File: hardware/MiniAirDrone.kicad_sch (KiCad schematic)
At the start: 26 parts, among them J1 USB_C_Receptacle_USB2.0, Q1 UMH3N, U1 CH340C, U2 ESP32-WROOM-32, U3 MPU-6050, U4 MS5611-01BA, U5 VL53L1CXV0FY1, U6 TS1117BCW33_RPG

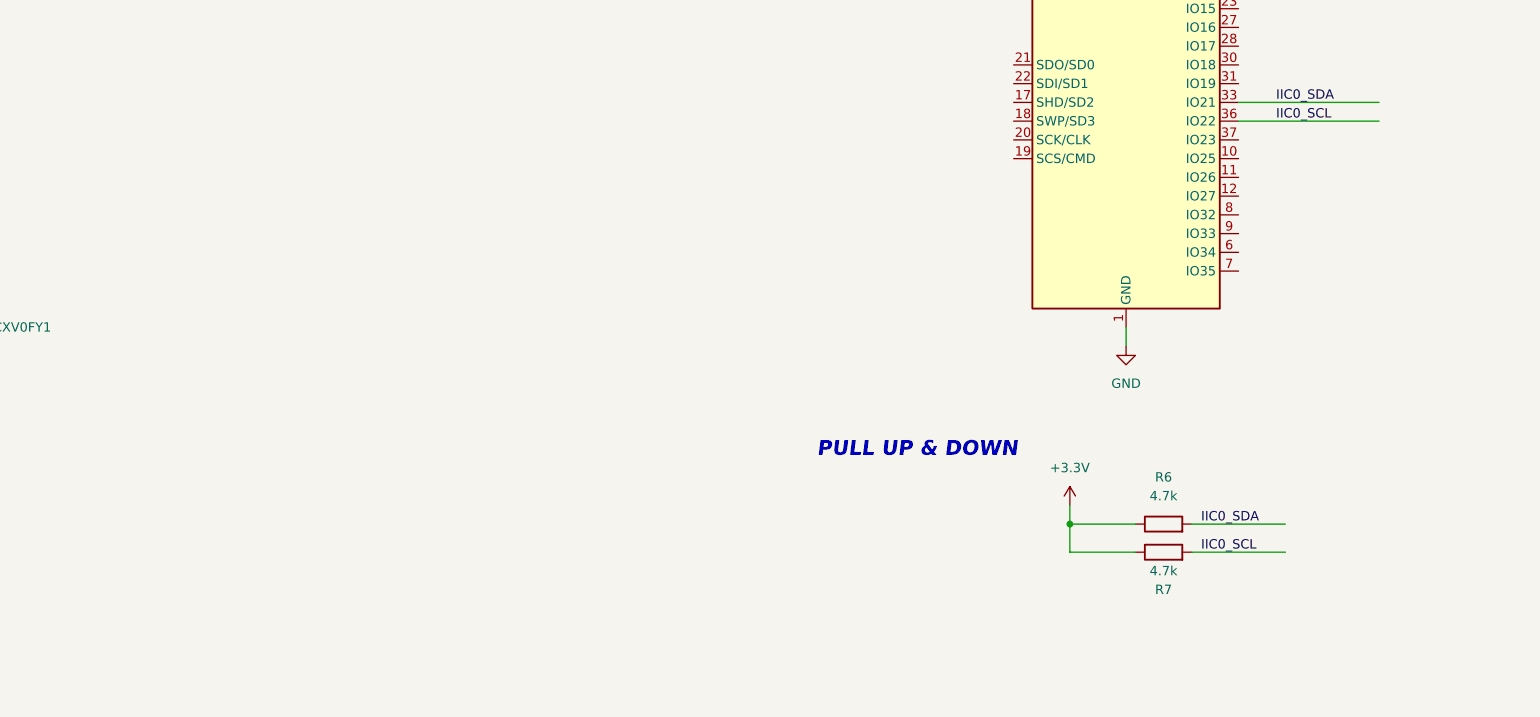
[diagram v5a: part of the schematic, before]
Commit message: new footprint and symbol
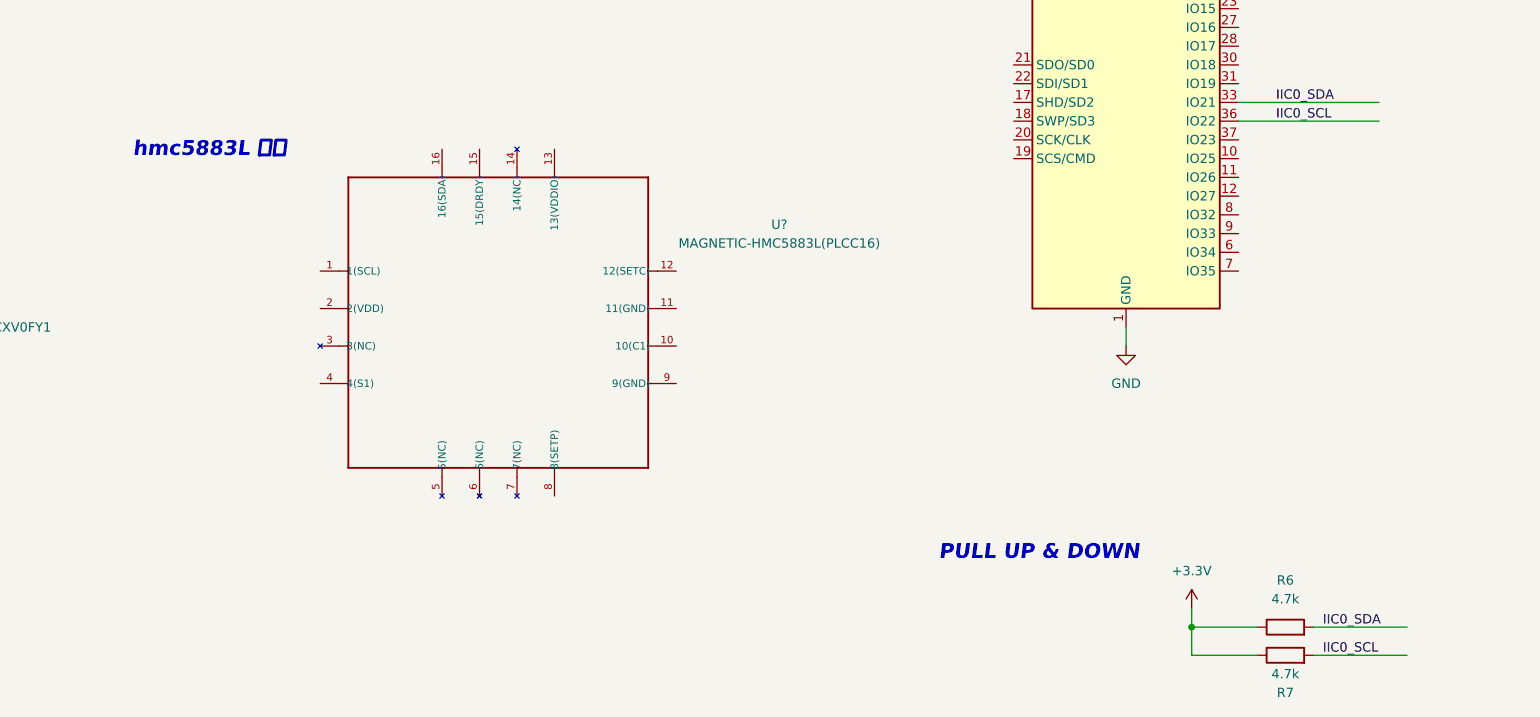
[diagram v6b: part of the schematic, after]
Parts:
- added U?: MAGNETIC-HMC5883L(PLCC16), PLCC16-0.5-3X3MM, symbol HMC5883L:MAGNETIC-HMC5883L(PLCC16)
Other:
- note added: "hmc5883L 罗盘"
- moved on the sheet: R6, R7
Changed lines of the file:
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@@
   (junction (at 49.53 41.91) (diameter 0) (color 0 0 0 0)
   )
-  (junction (at 350.52 134.62) (diameter 0) (color 0 0 0 0)
+  (junction (at 367.03 148.59) (diameter 0) (color 0 0 0 0)
   )
   (junction (at 116.84 91.44) (diameter 0) (color 0 0 0 0)
@@
     (stroke (width 0) (type default) (color 0 0 0 0))
   )
-  (wire (pts (xy 350.52 132.08) (xy 350.52 134.62))
+  (wire (pts (xy 367.03 146.05) (xy 367.03 148.59))
     (stroke (width 0) (type default) (color 0 0 0 0))
   )
@@
     (stroke (width 0) (type default) (color 0 0 0 0))
   )
-  (wire (pts (xy 367.03 134.62) (xy 379.73 134.62))
+  (wire (pts (xy 383.54 148.59) (xy 396.24 148.59))
     (stroke (width 0) (type default) (color 0 0 0 0))
   )
@@
     (stroke (width 0) (type default) (color 0 0 0 0))
   )
-  (wire (pts (xy 367.03 138.43) (xy 379.73 138.43))
+  (wire (pts (xy 383.54 152.4) (xy 396.24 152.4))
     (stroke (width 0) (type default) (color 0 0 0 0))
   )
@@
     (stroke (width 0) (type default) (color 0 0 0 0))
   )
-  (wire (pts (xy 350.52 134.62) (xy 359.41 134.62))
+  (wire (pts (xy 367.03 148.59) (xy 375.92 148.59))
     (stroke (width 0) (type default) (color 0 0 0 0))
   )
@@
     (stroke (width 0) (type default) (color 0 0 0 0))
   )
-  (wire (pts (xy 350.52 138.43) (xy 350.52 134.62))
+  (wire (pts (xy 367.03 152.4) (xy 367.03 148.59))
     (stroke (width 0) (type default) (color 0 0 0 0))
   )
@@
     (stroke (width 0) (type default) (color 0 0 0 0))
   )
-  (wire (pts (xy 359.41 138.43) (xy 350.52 138.43))
+  (wire (pts (xy 375.92 152.4) (xy 367.03 152.4))
     (stroke (width 0) (type default) (color 0 0 0 0))
   )
@@
     (effects (font (size 1.27 1.27)) (justify left bottom))
   )
+  (text "hmc5883L 罗盘" (at 223.52 85.09 0)
+    (effects (font (size 2.0066 2.0066) (thickness 0.4013) bold italic) (justify left bottom))
+  )
   (text "USB" (at 17.78 20.32 0)
     (effects (font (size 2.0066 2.0066) (thickness 0.4013) bold italic) (justify left bottom))
   )
-  (text "PULL UP & DOWN" (at 316.23 125.73 0)
+  (text "PULL UP & DOWN" (at 332.74 139.7 0)
     (effects (font (size 2.0066 2.0066) (thickness 0.4013) bold italic) (justify left bottom))
   )
@@
     (effects (font (size 1.27 1.27)) (justify left bottom))
   )
-  (label "IIC0_SDA" (at 368.3 134.62 0)
+  (label "IIC0_SDA" (at 384.81 148.59 0)
     (effects (font (size 1.27 1.27)) (justify left bottom))
   )
-  (label "IIC0_SCL" (at 368.3 138.43 0)
+  (label "IIC0_SCL" (at 384.81 152.4 0)
     (effects (font (size 1.27 1.27)) (justify left bottom))
   )
@@
     (pin "2")
   )
-  (symbol (lib_id "Device:R") (at 363.22 138.43 90) (unit 1)
-    (in_bom yes) (on_board yes)
-    (property "Reference" "R7" (id 0) (at 363.22 143.51 90))
-    (property "Value" "4.7k" (id 1) (at 363.22 140.97 90))
-    (property "Footprint" "" (id 2) (at 363.22 140.208 90)
-      (effects (font (size 1.27 1.27)) hide)
-    )
-    (property "Datasheet" "~" (id 3) (at 363.22 138.43 0)
+  (symbol (lib_id "Device:R") (at 379.73 152.4 90) (unit 1)
+    (in_bom yes) (on_board yes)
+    (property "Reference" "R7" (id 0) (at 379.73 157.48 90))
+    (property "Value" "4.7k" (id 1) (at 379.73 154.94 90))
+    (property "Footprint" "" (id 2) (at 379.73 154.178 90)
+      (effects (font (size 1.27 1.27)) hide)
+    )
+    (property "Datasheet" "~" (id 3) (at 379.73 152.4 0)
       (effects (font (size 1.27 1.27)) hide)
     )
@@
     )
     (pin "1")
+  )
+  (symbol (lib_id "HMC5883L:MAGNETIC-HMC5883L(PLCC16)") (at 273.05 107.95 0) (unit 1)
+    (in_bom yes) (on_board yes) (fields_autoplaced)
+    (property "Reference" "U?" (id 0) (at 311.15 94.0306 0))
+    (property "Value" "MAGNETIC-HMC5883L(PLCC16)" (id 1) (at 311.15 96.5706 0))
+    (property "Footprint" "PLCC16-0.5-3X3MM" (id 2) (at 273.05 107.95 0)
+      (effects (font (size 1.27 1.27)) (justify left bottom) hide)
+    )
+    (property "Datasheet" "" (id 3) (at 273.05 107.95 0)
+      (effects (font (size 1.27 1.27)) (justify left bottom) hide)
+    )
+    (property "MPN" "HMC5883L" (id 4) (at 273.05 107.95 0)
+      (effects (font (size 1.27 1.27)) (justify left bottom) hide)
+    )
+    (property "VALUE" "HMC5883L" (id 5) (at 273.05 107.95 0)
+      (effects (font (size 1.27 1.27)) (justify left bottom) hide)
+    )
+    (pin "1")
+    (pin "10")
+    (pin "11")
+    (pin "12")
+    (pin "13")
+    (pin "14")
+    (pin "15")
+    (pin "16")
+    (pin "2")
+    (pin "3")
+    (pin "4")
+    (pin "5")
+    (pin "6")
+    (pin "7")
+    (pin "8")
+    (pin "9")
   )
   (symbol (lib_id "Device:C_Small") (at 339.09 27.94 0) (unit 1)
@@
     (pin "2")
   )
-  (symbol (lib_id "Device:R") (at 363.22 134.62 90) (unit 1)
-    (in_bom yes) (on_board yes) (fields_autoplaced)
-    (property "Reference" "R6" (id 0) (at 363.22 128.27 90))
-    (property "Value" "4.7k" (id 1) (at 363.22 130.81 90))
-    (property "Footprint" "" (id 2) (at 363.22 136.398 90)
-      (effects (font (size 1.27 1.27)) hide)
-    )
-    (property "Datasheet" "~" (id 3) (at 363.22 134.62 0)
+  (symbol (lib_id "Device:R") (at 379.73 148.59 90) (unit 1)
+    (in_bom yes) (on_board yes) (fields_autoplaced)
+    (property "Reference" "R6" (id 0) (at 379.73 142.24 90))
+    (property "Value" "4.7k" (id 1) (at 379.73 144.78 90))
+    (property "Footprint" "" (id 2) (at 379.73 150.368 90)
+      (effects (font (size 1.27 1.27)) hide)
+    )
+    (property "Datasheet" "~" (id 3) (at 379.73 148.59 0)
       (effects (font (size 1.27 1.27)) hide)
     )
@@
     (pin "2")
   )
-  (symbol (lib_id "power:+3.3V") (at 350.52 132.08 0) (unit 1)
-    (in_bom yes) (on_board yes) (fields_autoplaced)
-    (property "Reference" "#PWR020" (id 0) (at 350.52 135.89 0)
-      (effects (font (size 1.27 1.27)) hide)
-    )
-    (property "Value" "+3.3V" (id 1) (at 350.52 127 0))
-    (property "Footprint" "" (id 2) (at 350.52 132.08 0)
-      (effects (font (size 1.27 1.27)) hide)
-    )
-    (property "Datasheet" "" (id 3) (at 350.52 132.08 0)
+  (symbol (lib_id "power:+3.3V") (at 367.03 146.05 0) (unit 1)
+    (in_bom yes) (on_board yes) (fields_autoplaced)
+    (property "Reference" "#PWR020" (id 0) (at 367.03 149.86 0)
+      (effects (font (size 1.27 1.27)) hide)
+    )
+    (property "Value" "+3.3V" (id 1) (at 367.03 140.97 0))
+    (property "Footprint" "" (id 2) (at 367.03 146.05 0)
+      (effects (font (size 1.27 1.27)) hide)
+    )
+    (property "Datasheet" "" (id 3) (at 367.03 146.05 0)
       (effects (font (size 1.27 1.27)) hide)
     )
@@
       (reference "U6") (unit 1) (value "TS1117BCW33_RPG") (footprint "Package_TO_SOT_SMD:SOT-223-3_TabPin2")
     )
-  )
+    (path "/3bb6b5f0-d722-439c-972e-7102e551e716"
+      (reference "U?") (unit 1) (value "MAGNETIC-HMC5883L(PLCC16)") (footprint "PLCC16-0.5-3X3MM")
+    )
+  )

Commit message: navigator
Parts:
- added C?: 475, symbol Device:C
- added C?: 224, symbol Device:C
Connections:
- net GND: now also U?.11 (11(GND)), U?.9 (9(GND)), C?.2
- net at U?.10 (10(C1)): now also C?.1
- net at U?.12 (12(SETC)): now also C?.2
- net at U?.8 (8(SETP)): now also C?.1
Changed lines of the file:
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@@
   (junction (at 168.91 30.48) (diameter 0) (color 0 0 0 0)
   )
+  (junction (at 308.61 110.49) (diameter 0) (color 0 0 0 0)
+  )
   (junction (at 237.49 45.72) (diameter 0) (color 0 0 0 0)
   )
   (junction (at 116.84 113.03) (diameter 0) (color 0 0 0 0)
+  )
+  (junction (at 308.61 115.57) (diameter 0) (color 0 0 0 0)
   )
   (junction (at 330.2 25.4) (diameter 0) (color 0 0 0 0)
@@
     (stroke (width 0) (type default) (color 0 0 0 0))
   )
+  (wire (pts (xy 312.42 100.33) (xy 297.18 100.33))
+    (stroke (width 0) (type default) (color 0 0 0 0))
+  )
   (wire (pts (xy 189.23 91.44) (xy 189.23 88.9))
     (stroke (width 0) (type default) (color 0 0 0 0))
@@
     (stroke (width 0) (type default) (color 0 0 0 0))
   )
+  (wire (pts (xy 280.67 130.81) (xy 280.67 133.35))
+    (stroke (width 0) (type default) (color 0 0 0 0))
+  )
   (wire (pts (xy 106.68 106.68) (xy 106.68 113.03))
     (stroke (width 0) (type default) (color 0 0 0 0))
   )
+  (wire (pts (xy 308.61 110.49) (xy 308.61 115.57))
+    (stroke (width 0) (type default) (color 0 0 0 0))
+  )
   (wire (pts (xy 358.14 107.95) (xy 358.14 110.49))
     (stroke (width 0) (type default) (color 0 0 0 0))
@@
     (stroke (width 0) (type default) (color 0 0 0 0))
   )
+  (wire (pts (xy 308.61 115.57) (xy 308.61 119.38))
+    (stroke (width 0) (type default) (color 0 0 0 0))
+  )
   (wire (pts (xy 185.42 43.18) (xy 185.42 53.34))
     (stroke (width 0) (type default) (color 0 0 0 0))
@@
     (stroke (width 0) (type default) (color 0 0 0 0))
   )
+  (wire (pts (xy 297.18 105.41) (xy 308.61 105.41))
+    (stroke (width 0) (type default) (color 0 0 0 0))
+  )
   (wire (pts (xy 34.29 67.31) (xy 26.67 67.31))
     (stroke (width 0) (type default) (color 0 0 0 0))
@@
     (stroke (width 0) (type default) (color 0 0 0 0))
   )
+  (wire (pts (xy 303.53 133.35) (xy 312.42 133.35))
+    (stroke (width 0) (type default) (color 0 0 0 0))
+  )
+  (wire (pts (xy 312.42 133.35) (xy 312.42 100.33))
+    (stroke (width 0) (type default) (color 0 0 0 0))
+  )
   (wire (pts (xy 106.68 91.44) (xy 116.84 91.44))
     (stroke (width 0) (type default) (color 0 0 0 0))
@@
     (stroke (width 0) (type default) (color 0 0 0 0))
   )
+  (wire (pts (xy 280.67 133.35) (xy 295.91 133.35))
+    (stroke (width 0) (type default) (color 0 0 0 0))
+  )
+  (wire (pts (xy 307.34 110.49) (xy 308.61 110.49))
+    (stroke (width 0) (type default) (color 0 0 0 0))
+  )
+  (wire (pts (xy 308.61 105.41) (xy 308.61 110.49))
+    (stroke (width 0) (type default) (color 0 0 0 0))
+  )
   (wire (pts (xy 92.71 104.14) (xy 106.68 104.14))
     (stroke (width 0) (type default) (color 0 0 0 0))
@@
     (stroke (width 0) (type default) (color 0 0 0 0))
   )
+  (wire (pts (xy 297.18 115.57) (xy 308.61 115.57))
+    (stroke (width 0) (type default) (color 0 0 0 0))
+  )
   (wire (pts (xy 34.29 67.31) (xy 34.29 68.58))
     (stroke (width 0) (type default) (color 0 0 0 0))
@@
   )
   (wire (pts (xy 116.84 111.76) (xy 116.84 113.03))
+    (stroke (width 0) (type default) (color 0 0 0 0))
+  )
+  (wire (pts (xy 297.18 110.49) (xy 299.72 110.49))
     (stroke (width 0) (type default) (color 0 0 0 0))
   )
@@
     )
     (property "Datasheet" "" (id 3) (at 189.23 125.73 0)
+      (effects (font (size 1.27 1.27)) hide)
+    )
+    (pin "1")
+  )
+  (symbol (lib_id "power:GND") (at 308.61 119.38 0) (unit 1)
+    (in_bom yes) (on_board yes) (fields_autoplaced)
+    (property "Reference" "#PWR?" (id 0) (at 308.61 125.73 0)
+      (effects (font (size 1.27 1.27)) hide)
+    )
+    (property "Value" "GND" (id 1) (at 308.61 124.46 0))
+    (property "Footprint" "" (id 2) (at 308.61 119.38 0)
+      (effects (font (size 1.27 1.27)) hide)
+    )
+    (property "Datasheet" "" (id 3) (at 308.61 119.38 0)
       (effects (font (size 1.27 1.27)) hide)
     )
@@
     (pin "5")
   )
+  (symbol (lib_id "Device:C") (at 303.53 110.49 90) (unit 1)
+    (in_bom yes) (on_board yes)
+    (property "Reference" "C?" (id 0) (at 304.8 106.68 90))
+    (property "Value" "475" (id 1) (at 306.07 109.22 90))
+    (property "Footprint" "" (id 2) (at 307.34 109.5248 0)
+      (effects (font (size 1.27 1.27)) hide)
+    )
+    (property "Datasheet" "~" (id 3) (at 303.53 110.49 0)
+      (effects (font (size 1.27 1.27)) hide)
+    )
+    (pin "1")
+    (pin "2")
+  )
   (symbol (lib_id "Regulator_Linear:TS1117BCW33_RPG") (at 288.29 44.45 0) (unit 1)
     (in_bom yes) (on_board yes)
@@
     (pin "1")
   )
+  (symbol (lib_id "Device:C") (at 299.72 133.35 90) (unit 1)
+    (in_bom yes) (on_board yes) (fields_autoplaced)
+    (property "Reference" "C?" (id 0) (at 299.72 125.73 90))
+    (property "Value" "224" (id 1) (at 299.72 128.27 90))
+    (property "Footprint" "" (id 2) (at 303.53 132.3848 0)
+      (effects (font (size 1.27 1.27)) hide)
+    )
+    (property "Datasheet" "~" (id 3) (at 299.72 133.35 0)
+      (effects (font (size 1.27 1.27)) hide)
+    )
+    (pin "1")
+    (pin "2")
+  )
   (sheet_instances
     (path "/" (page "1"))
@@
       (reference "#PWR0104") (unit 1) (value "+3.3V") (footprint "")
     )
+    (path "/1cee6a59-d3a0-4f59-bd50-d39a8b45bae5"
+      (reference "#PWR?") (unit 1) (value "GND") (footprint "")
+    )
     (path "/d909e2e9-9c77-4bae-a3fd-5677733b7e62"
       (reference "C1") (unit 1) (value "0.1uF") (footprint "Capacitor_SMD:C_0603_1608Metric")
@@
       (reference "C7") (unit 1) (value "0.1uF") (footprint "")
     )
+    (path "/de92b927-d8f0-4a79-a08f-1fc452b3ad3d"
+      (reference "C?") (unit 1) (value "475") (footprint "")
+    )
+    (path "/f7525221-6f5a-454f-bc0d-fecc3a240294"
+      (reference "C?") (unit 1) (value "224") (footprint "")
+    )
     (path "/b74a2c11-24dd-463c-aa73-ee48758aca8f"
